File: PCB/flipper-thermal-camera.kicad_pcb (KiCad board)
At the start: 2 copper layers, 67 x 25.2 mm, 27 parts, among them IC1 VEML7700-TT, J1 Conn_01x08, J2 Conn_01x10, U1 MLX90640ESF-BAB-000-SP, U2 XC6206PxxxMR, U3 ICM-20948, U4 SHT31-DIS

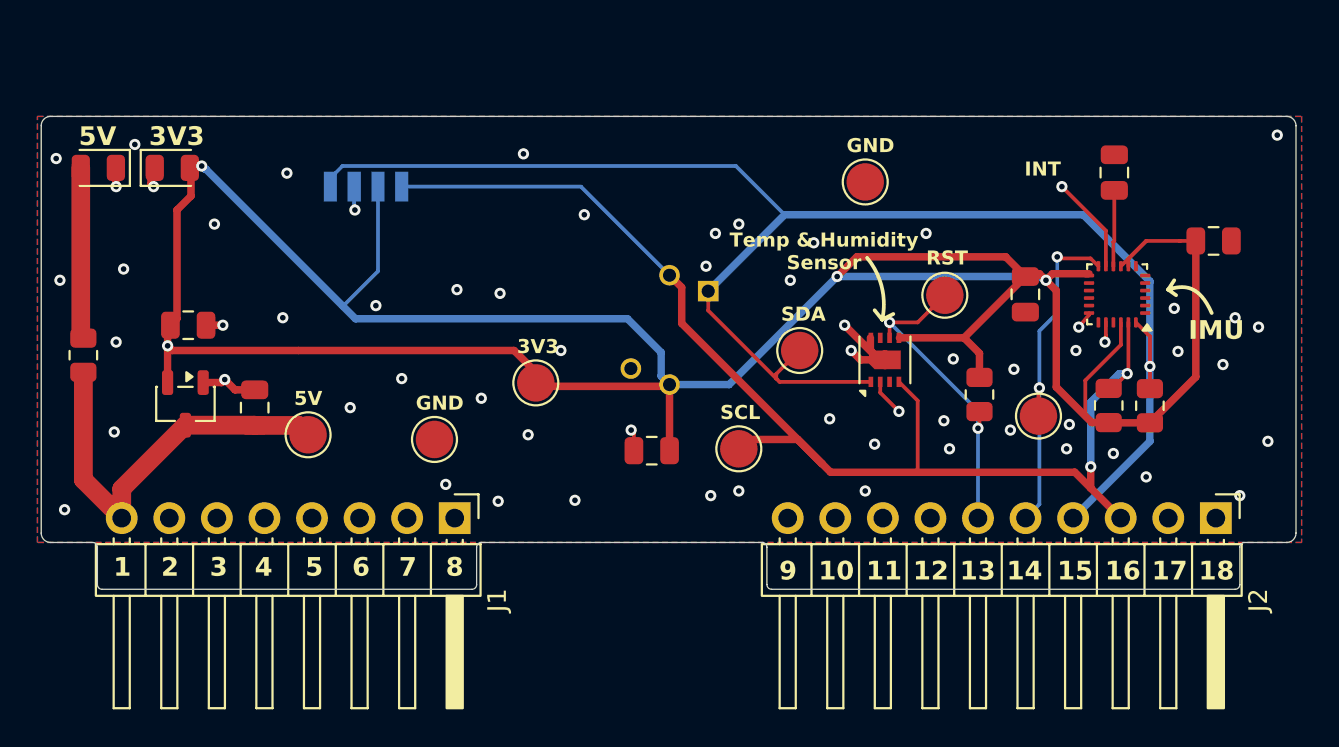
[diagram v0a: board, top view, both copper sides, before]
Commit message: switch IMU and add more capacitors and diodes
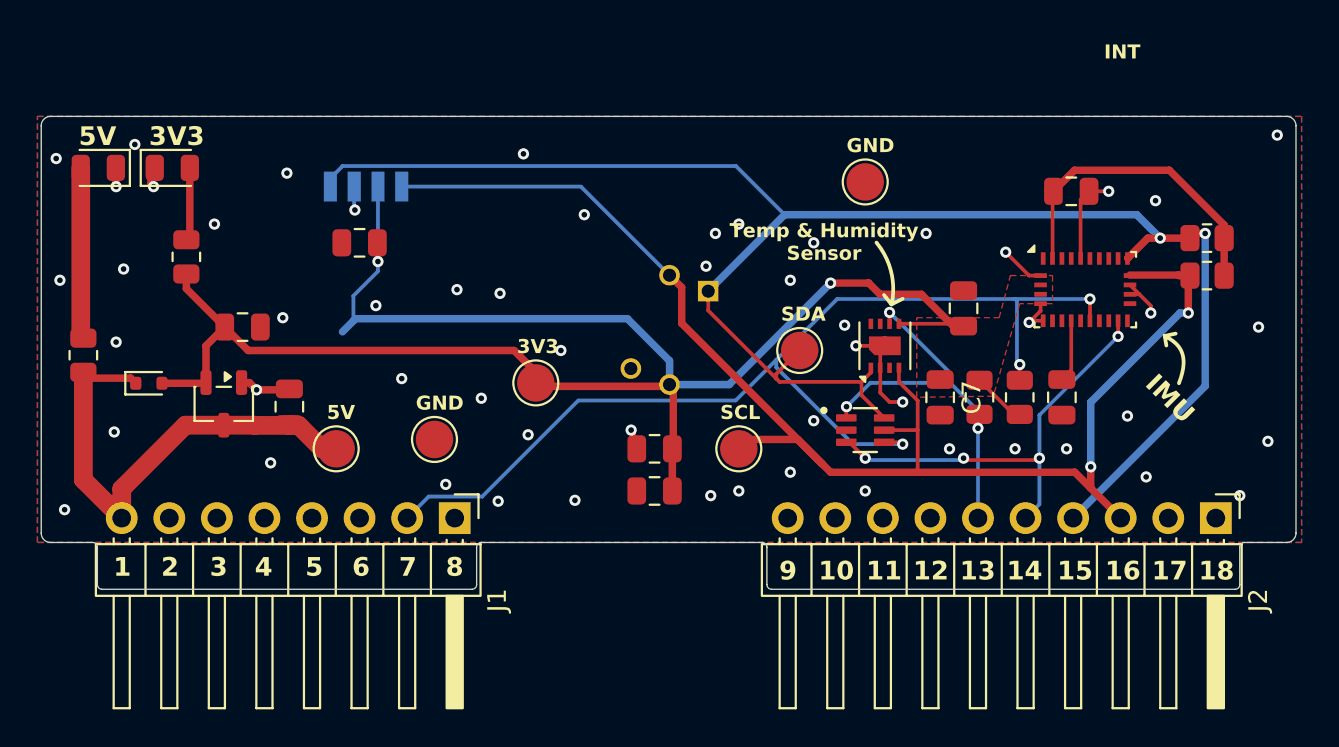
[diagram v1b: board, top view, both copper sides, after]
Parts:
- removed TP6: TMP_SENS_RST, TestPoint:TestPoint_Pad_D2.0mm
- removed TP7: INT_ICM, TestPoint:TestPoint_Pad_D2.0mm
- added C7: 100nF, Capacitor_SMD:C_0805_2012Metric, F.Cu at (136.0, 99.2)
- added C8: 10uF, Capacitor_SMD:C_0805_2012Metric, F.Cu at (105.0, 91.0)
- added C9: 10uF, Capacitor_SMD:C_0805_2012Metric, F.Cu at (120.8, 104.2)
- added D3: RB521S-30, Diode_SMD:D_SOD-523, F.Cu at (93.8, 98.5)
- added R5: 10k, Resistor_SMD:R_0805_2012Metric, F.Cu at (140.2, 99.2)
- added R6: 330, Resistor_SMD:R_0805_2012Metric, F.Cu at (95.8, 91.8)
- added U6: SP1001-05JTG, Components:SOP65P220X110-6N, F.Cu at (132.0, 101.0)
- C1: value 100nF -> 120nF
- C3: value 100nF -> 1uF
- SDA1: value GND -> SDA_TP
- U3: value ICM-20948 -> BNO055; footprint Sensor_Motion:InvenSense_QFN-24_3x3mm_P0.4mm -> Package_LGA:LGA-28_5.2x3.8mm_P0.5mm
- moved C3 12.3 mm to (142.5, 99.2)
- moved R2 9.46 mm to (150.2, 90.8), turned to 180 degrees
- moved R1 8.70 mm to (150.2, 92.8), turned to 180 degrees
- moved C1 8.05 mm to (143.0, 88.2)
- moved C2 3.38 mm to (137.2, 94.5), turned to -90 degrees
- moved C6 2.90 mm to (98.8, 95.5)
- moved U2 2.05 mm to (97.8, 99.6)
- moved C5 1.85 mm to (101.2, 99.8)
- moved U3 1.72 mm to (143.8, 93.5), turned to 0 degrees
- moved TP2 1.68 mm to (103.8, 102.0)
- moved U4 0.75 mm to (133.1, 96.5)
- moved C4 0.18 mm to (120.8, 102.0)
- moved R4 0.15 mm to (138.1, 99.2)
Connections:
- C3 pad 1: Net-(U3-REGOUT) -> GND
- C3 pad 2: GND -> Net-(U3-CAP)
- D2 pad 2: +3V3 -> Net-(D2-A)
- J1 pad 2: unconnected-(J1-Pin_2-Pad2) -> /nRESET
- U3 pad 10: Net-(U3-REGOUT) -> unconnected-(U3-BL_IND-Pad10)
- U3 pad 11: GND -> /nRESET
- U3 pad 12: /INT_1 -> unconnected-(U3-PIN12-Pad12)
- U3 pad 13: +3V3 -> unconnected-(U3-PIN13-Pad13)
- U3 pad 14: unconnected-(U3-NC-Pad14) -> /INT_1
- U3 pad 17: unconnected-(U3-NC-Pad17) -> GND
- U3 pad 19: unconnected-(U3-RESV-Pad19) -> /SCL
- U3 pad 2: unconnected-(U3-NC-Pad2) -> GND
- U3 pad 20: GND -> /SDA
- U3 pad 22: +3V3 -> unconnected-(U3-PIN22-Pad22)
- U3 pad 23: /SCL -> unconnected-(U3-PIN23-Pad23)
- U3 pad 24: /SDA -> unconnected-(U3-PIN24-Pad24)
- U3 pad 3: unconnected-(U3-NC-Pad3) -> +3V3
- U3 pad 4: unconnected-(U3-NC-Pad4) -> +3V3
- U3 pad 5: unconnected-(U3-NC-Pad5) -> GND
- U3 pad 6: unconnected-(U3-NC-Pad6) -> GND
- U3 pad 8: +3V3 -> unconnected-(U3-PIN8-Pad8)
- U3 pad 9: +3V3 -> Net-(U3-CAP)
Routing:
- net /nRESET: track 0.00 -> 56.8 mm, vias 0 -> 3
- net +3V3: track 163.6 -> 111.7 mm, vias 4 -> 2
- net /SCL: track 67.9 -> 76.4 mm
- net /SDA: track 84.3 -> 91.4 mm, vias 1 -> 2
- net +5V: track 21.8 -> 26.7 mm
- net /INT_1: track 18.6 -> 23.4 mm, vias 2 -> 4
- net Net-(U3-REGOUT): track 4.07 -> 0.00 mm
- net Net-(D2-A): track 0.00 -> 3.92 mm
- net Net-(U3-CAP): track 0.00 -> 3.34 mm
- net /TMP_RST: track 17.7 -> 21.0 mm, vias 2 -> 3
- net GND: track 23.7 -> 24.5 mm, vias 64 -> 56
- added copper zone on F.Cu, net +3V3
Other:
- board text removed: "RST"

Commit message: fix up wiring
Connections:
- U4 pad 7: unconnected-(U4-R-Pad7) -> GND
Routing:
- net GND: track 24.5 -> 35.0 mm, vias 56 -> 58
- net +3V3: track 111.7 -> 115.2 mm
- net /nRESET: track 56.8 -> 55.1 mm
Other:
- board text added: "evanyu.dev"
- board text removed: "INT"
